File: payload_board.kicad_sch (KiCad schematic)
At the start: 92 parts, among them IC1 RP2040_QFN56, IC2 AZ1117CH-3.3TRG1, J1 Cam_PicoLock, J12 5025700893, J15 Debug_Conn, J2 Cam_Conn, J3 Antenna_Conn, J4 usb jumper, J5 Display_Conn, J7 Breakout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

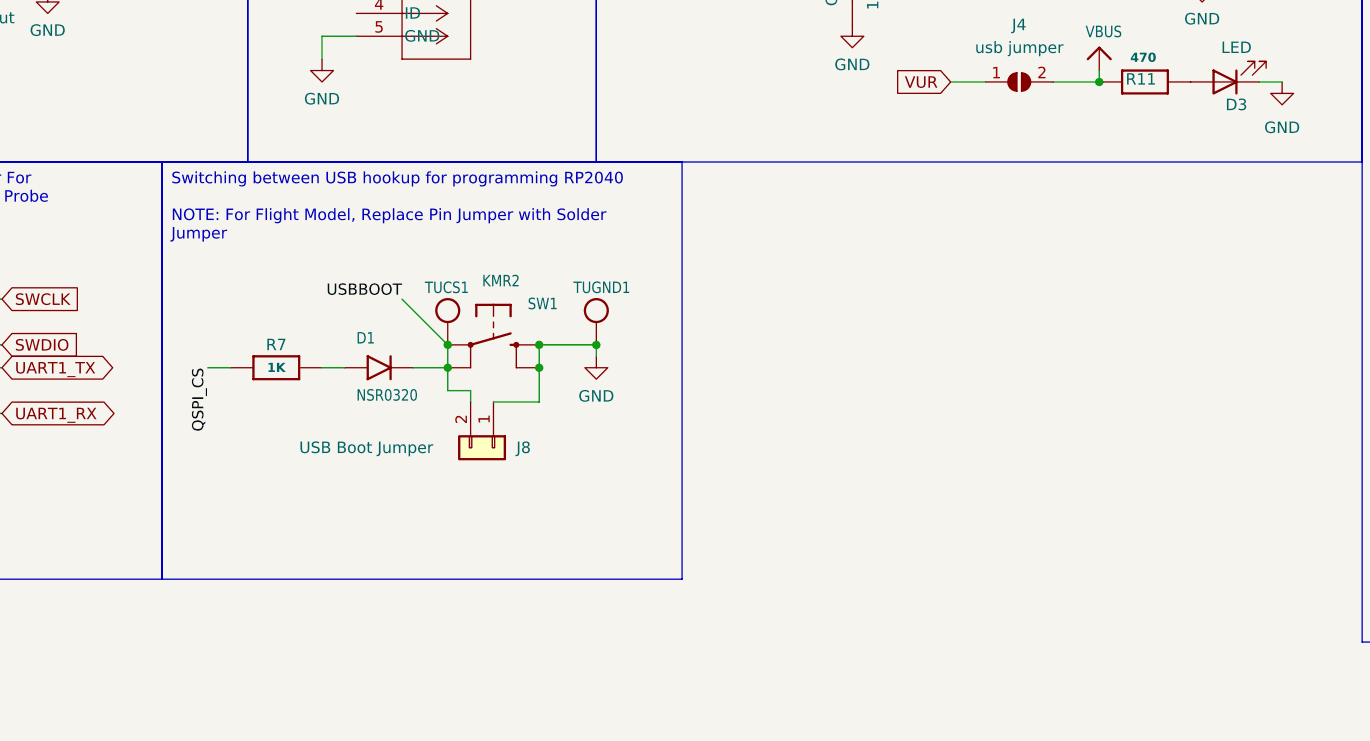
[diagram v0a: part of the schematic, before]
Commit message: Updated component placements and footprints
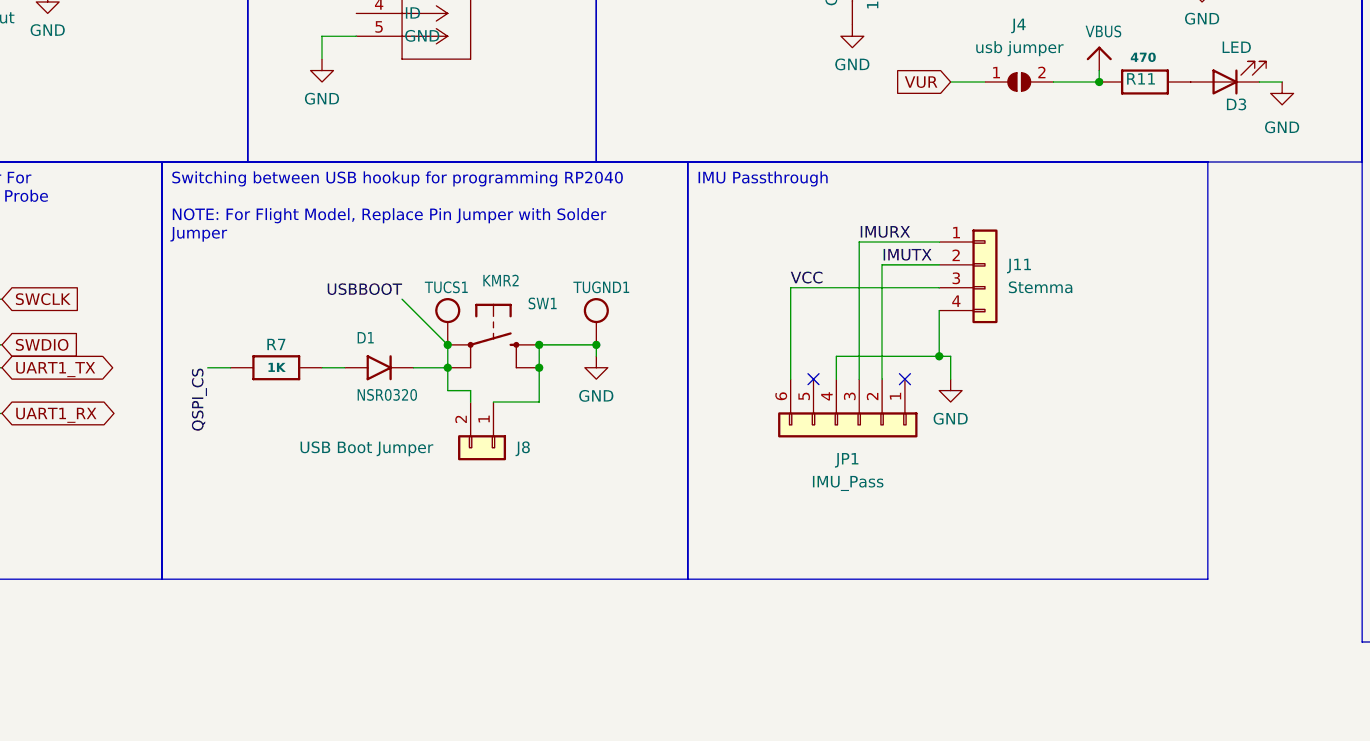
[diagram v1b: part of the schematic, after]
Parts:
- added J11: Stemma, symbol Connector_Generic:Conn_01x04
- added JP1: IMU_Pass, symbol Connector_Generic:Conn_01x06
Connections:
- net GND: now also J11.4 (Pin_4), JP1.4 (Pin_4)
- new net IMURX: J11.1 (Pin_1), JP1.3 (Pin_3)
- new net IMUTX: J11.2 (Pin_2), JP1.2 (Pin_2)
- new net VCC: J11.3 (Pin_3), JP1.6 (Pin_6)
- no-connect marks 7 -> 9

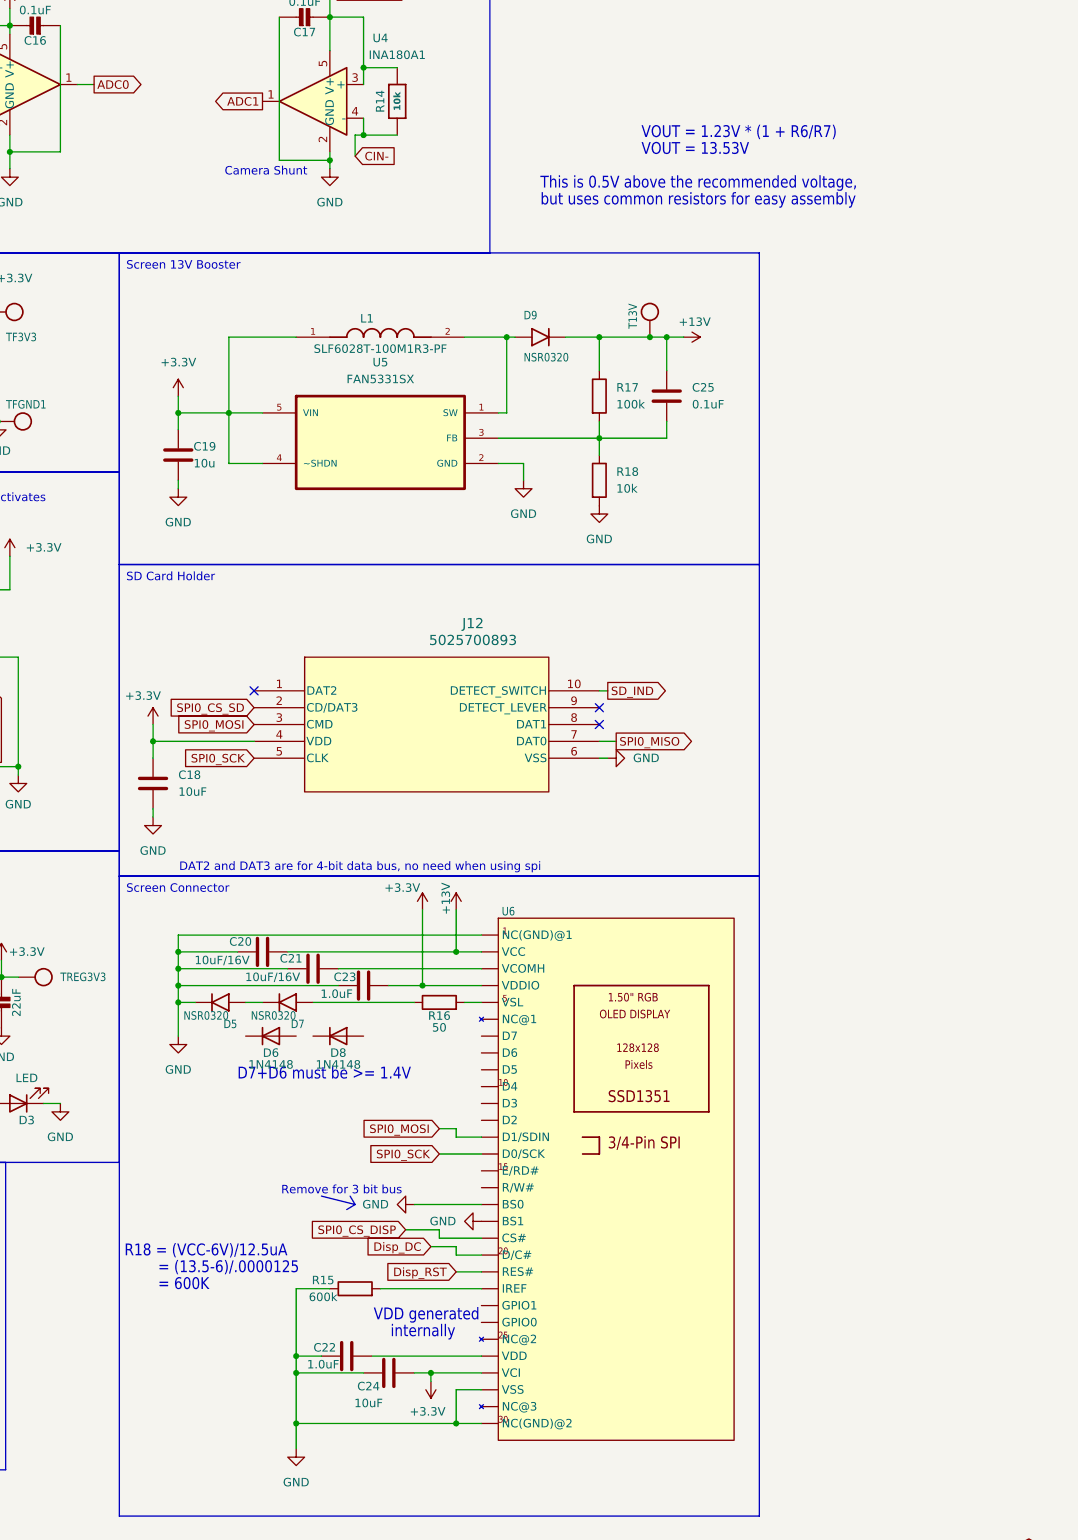
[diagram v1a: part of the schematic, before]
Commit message: Updated display footprints to reflect avaliability
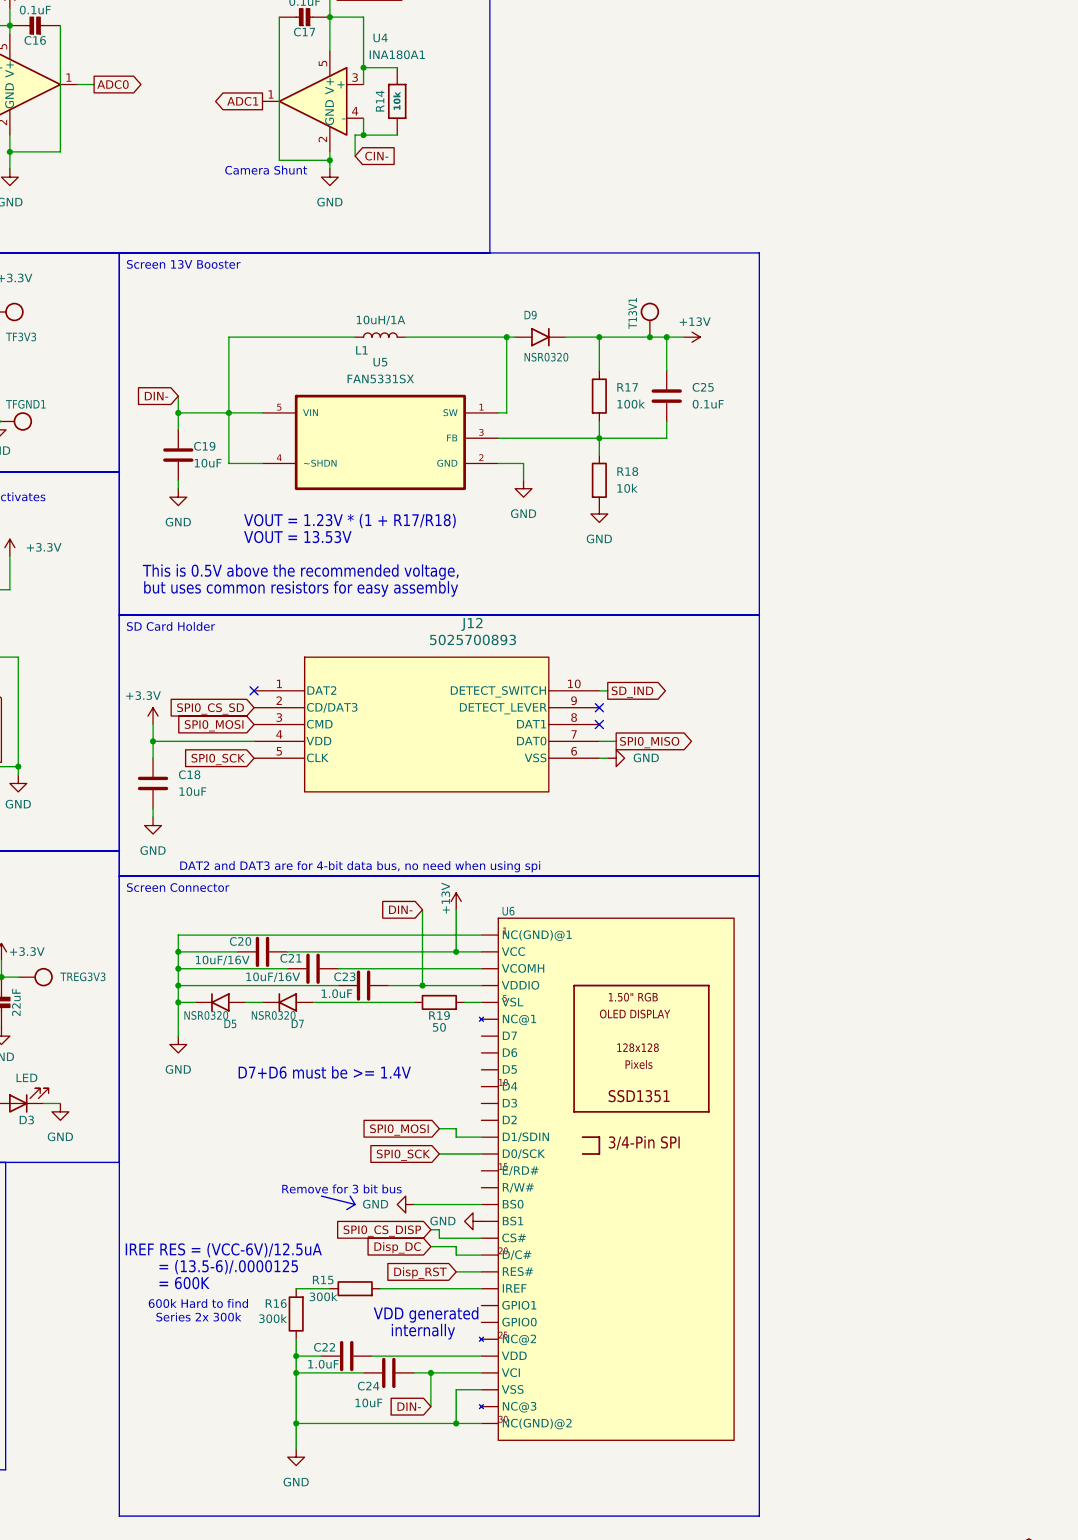
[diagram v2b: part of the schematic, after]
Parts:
- removed D6, D8: 1N4148, Diode_THT:D_DO-35_SOD27_P7.62mm_Horizontal, symbol Diode:1N4148
- added R16: 300k, Resistor_SMD:R_0603_1608Metric_Pad0.98x0.95mm_HandSolder, symbol Device:R
- C19: value 10u -> 10uF
- L1: value SLF6028T-100M1R3-PF -> 10uH/1A; footprint PayloadBoard:IND_SLF6028T-100M1R3-PF -> Inductor_SMD:L_1008_2520Metric_Pad1.43x2.20mm_HandSolder; symbol PayloadBoard:SLF6028T-100M1R3-PF -> Device:L
- R15: value 600k -> 300k
- renumbered R16 to R19, T13V to T13V1
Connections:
- net +3.3V: no longer C19.1, C23.2, C24.2, L1.1, U5.4 (~SHDN), U5.5 (VIN), U6.P$27 (VDDIO), U6.P$4 (VCI)
- net DIN-: now also C19.1, C23.2, C24.2, L1.1, U5.4 (~SHDN), U5.5 (VIN), U6.P$27 (VDDIO), U6.P$4 (VCI)
- net GND: now also R16.1; no longer R15.1
- new net: R15.1, R16.2
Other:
- note added: "600k Hard to find Series 2x 300k"
- note added: "IREF RES = (VCC-6V)/12.5uA"
- note added: "VOUT = 1.23V * (1 + R17/R18)"
- note removed: "R18 = (VCC-6V)/12.5uA"
- note removed: "VOUT = 1.23V * (1 + R6/R7)"
